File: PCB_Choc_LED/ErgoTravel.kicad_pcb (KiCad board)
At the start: 2 copper layers, 137.9 x 92.7 mm, 195 parts, among them J1 Conn_01x05, J10 Conn_01x01, J11 Conn_01x01, J12 Conn_01x01, J13 Conn_01x02, J14 Conn_01x02, J2 Audio-Jack-4, J3 Audio-Jack-4, J4 Conn_01x06, J5 Conn_01x01, J6 Conn_01x01, J7 Conn_01x01, J8 Conn_01x01, J9 Conn_01x01, K1 KEYSW, K10 KEYSW, K11 KEYSW, K12 KEYSW, K13 KEYSW, K14 KEYSW, K15 KEYSW, K16 KEYSW, K17 KEYSW, K18 KEYSW, K19 KEYSW, K2 KEYSW, K20 KEYSW, K21 KEYSW, K22 KEYSW, K23 KEYSW, K24 KEYSW, K26 KEYSW, K27 KEYSW, K28 KEYSW, K3 KEYSW, K4 KEYSW, K5 KEYSW, K6 KEYSW, K7 KEYSW, K8 KEYSW, K9 KEYSW, Q1 2N7002, Q2 2N7002, SW1 SW_PUSH, SW2 SW_PUSH, SW3 SW_SPDT, SW4 SW_SPDT, U1 ProMicro

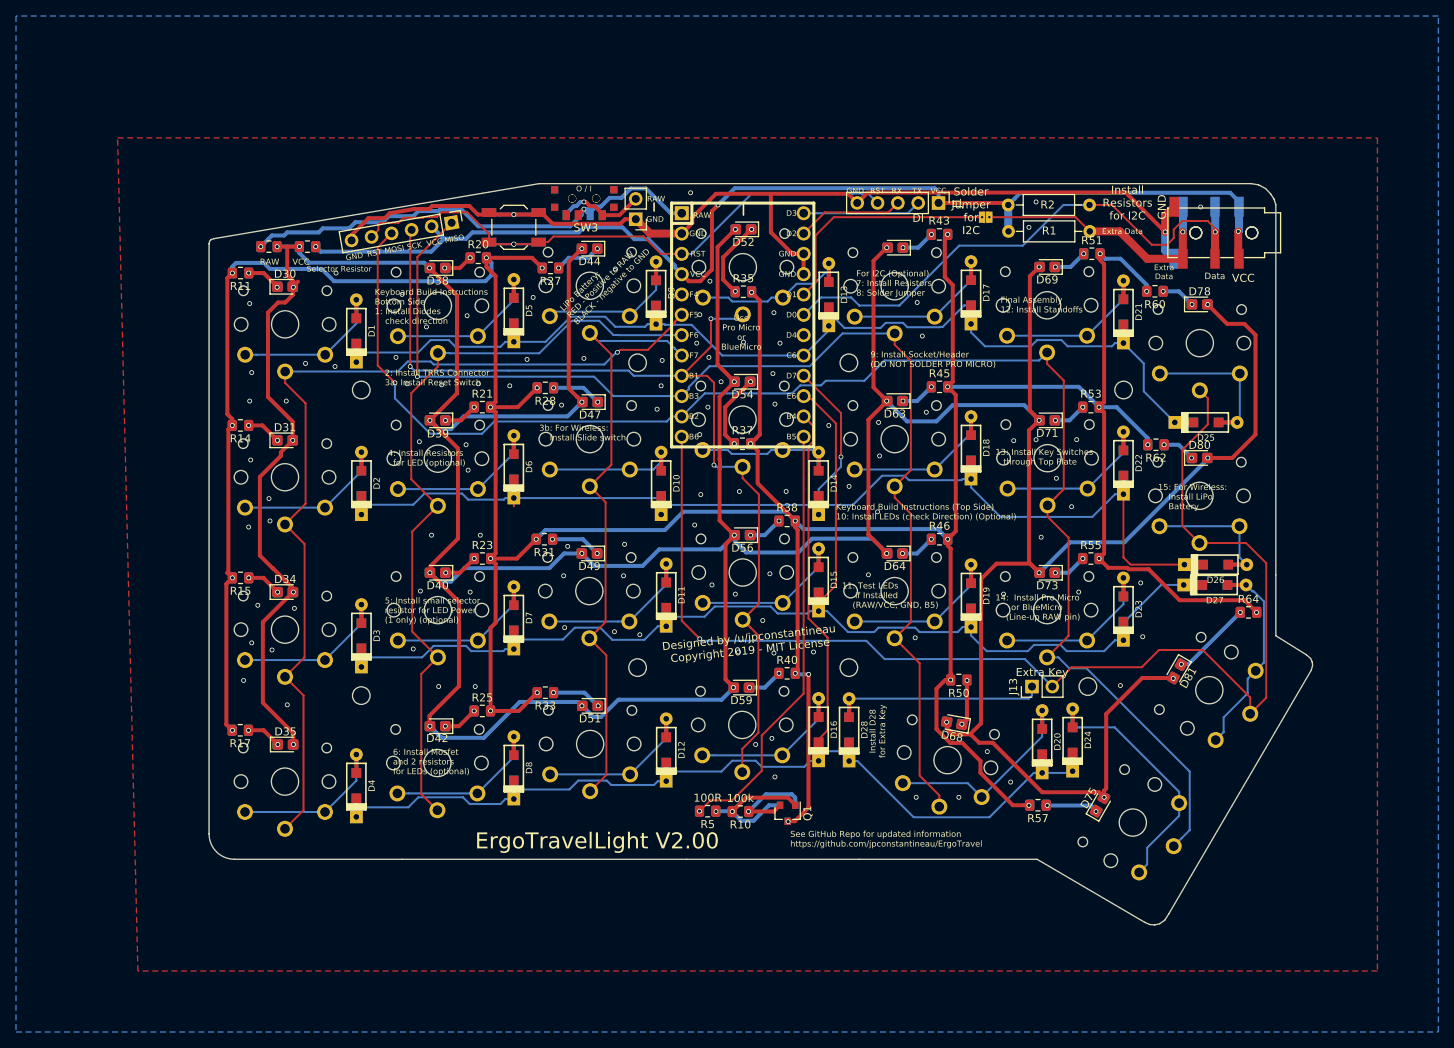
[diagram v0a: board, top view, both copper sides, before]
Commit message: adding prototype for mids
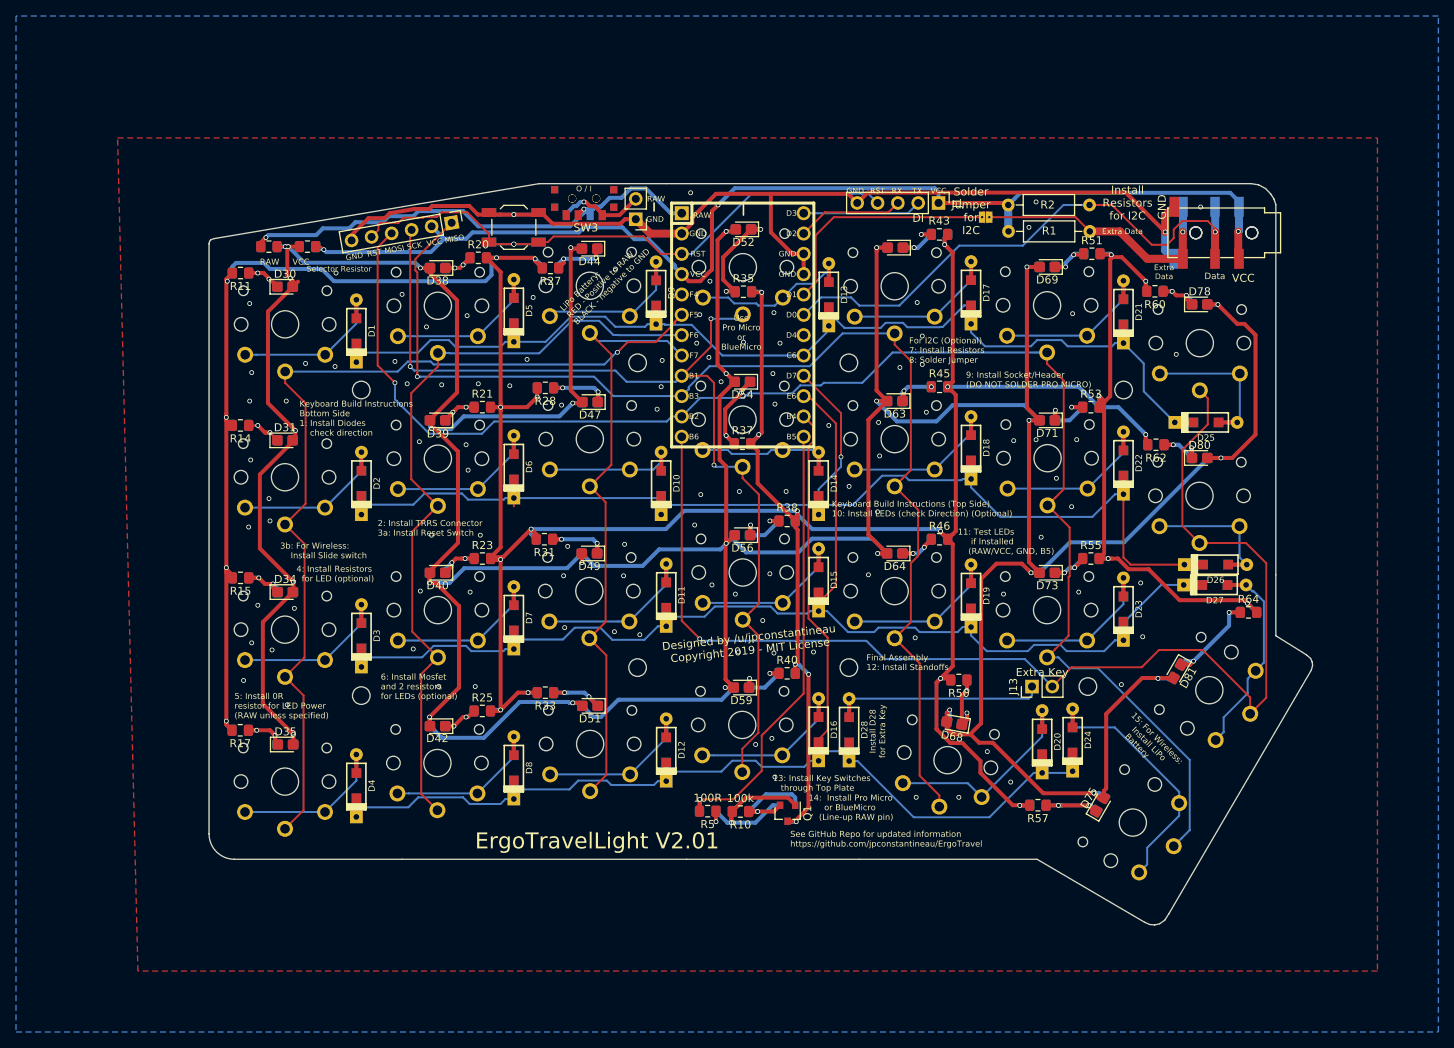
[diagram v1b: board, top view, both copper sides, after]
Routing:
- net /LEDPOWER: track 603.7 -> 656.6 mm
- net /LEDDRIVER: track 488.6 -> 541.1 mm
- net Net-(D75-Pad1): track 6.42 -> 13.3 mm
- net Net-(Q1-Pad1): track 18.3 -> 24.1 mm
- net Net-(D71-Pad1): track 4.16 -> 9.52 mm
- net Net-(D56-Pad1): track 4.34 -> 9.19 mm
- net Net-(D67-Pad1): track 5.79 -> 10.6 mm
- net Net-(D52-Pad1): track 9.87 -> 14.6 mm
- net Net-(D58-Pad1): track 4.46 -> 9.06 mm
- net Net-(D48-Pad1): track 6.31 -> 10.6 mm
- net Net-(D81-Pad1): track 10.0 -> 14.2 mm
- net Net-(D60-Pad1): track 4.23 -> 8.14 mm
- net Net-(D79-Pad1): track 4.17 -> 7.88 mm
- net Net-(D44-Pad1): track 5.84 -> 9.33 mm
- net Net-(D54-Pad1): track 9.53 -> 12.8 mm
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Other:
- board text added: "5: Install 0R resistor for LED Power (RAW unless specified)"
- board text added: "ErgoTravelLight V2.01"
- board text removed: "5: Install small selector resistor for LED Power (1 only) (optional)"
- board text removed: "ErgoTravelLight V2.00"
